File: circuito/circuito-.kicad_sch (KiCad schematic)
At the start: 15 parts, among them Q1 IRF9540 P, Q2 2N3904 / BC547, U3 TXS0108EPW, U4 TPSM53602RDA

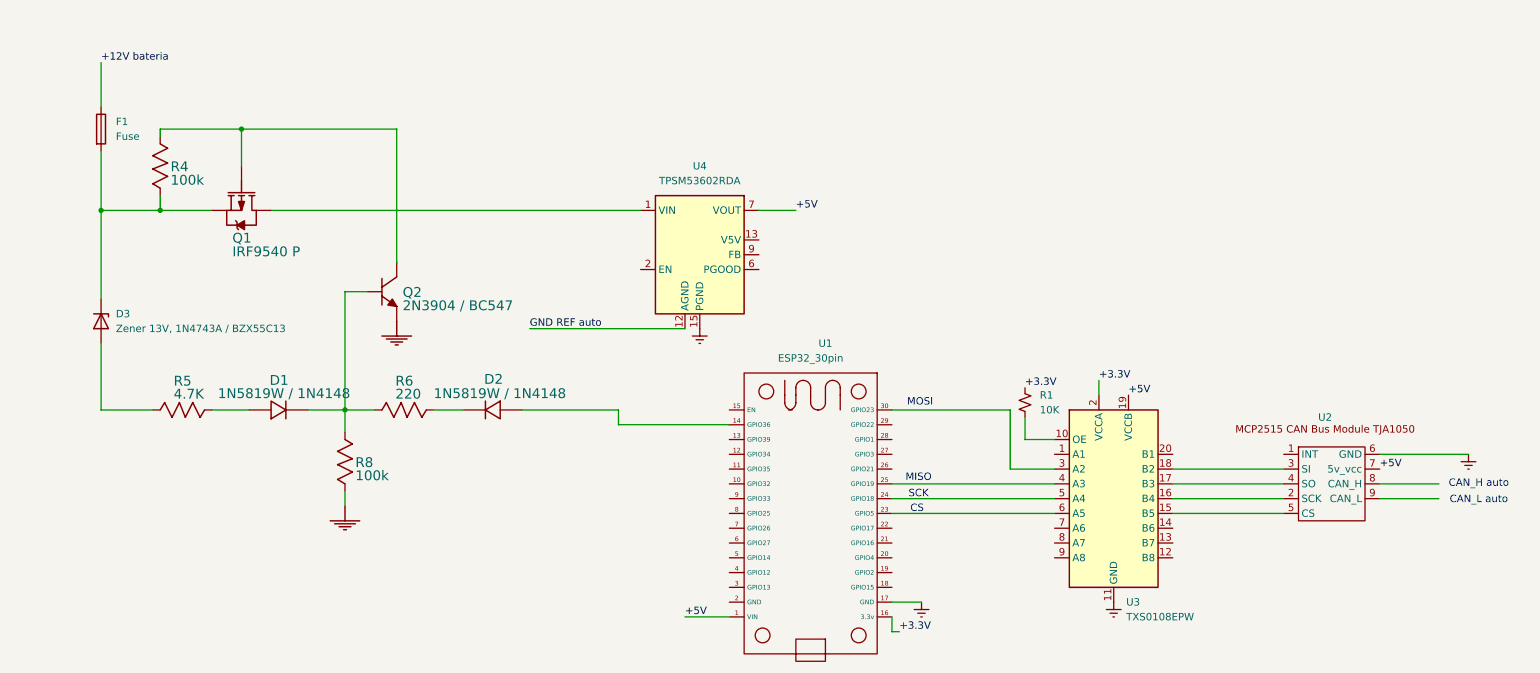
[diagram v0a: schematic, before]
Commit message: proteccion de picos del circuito, unificacion de masas
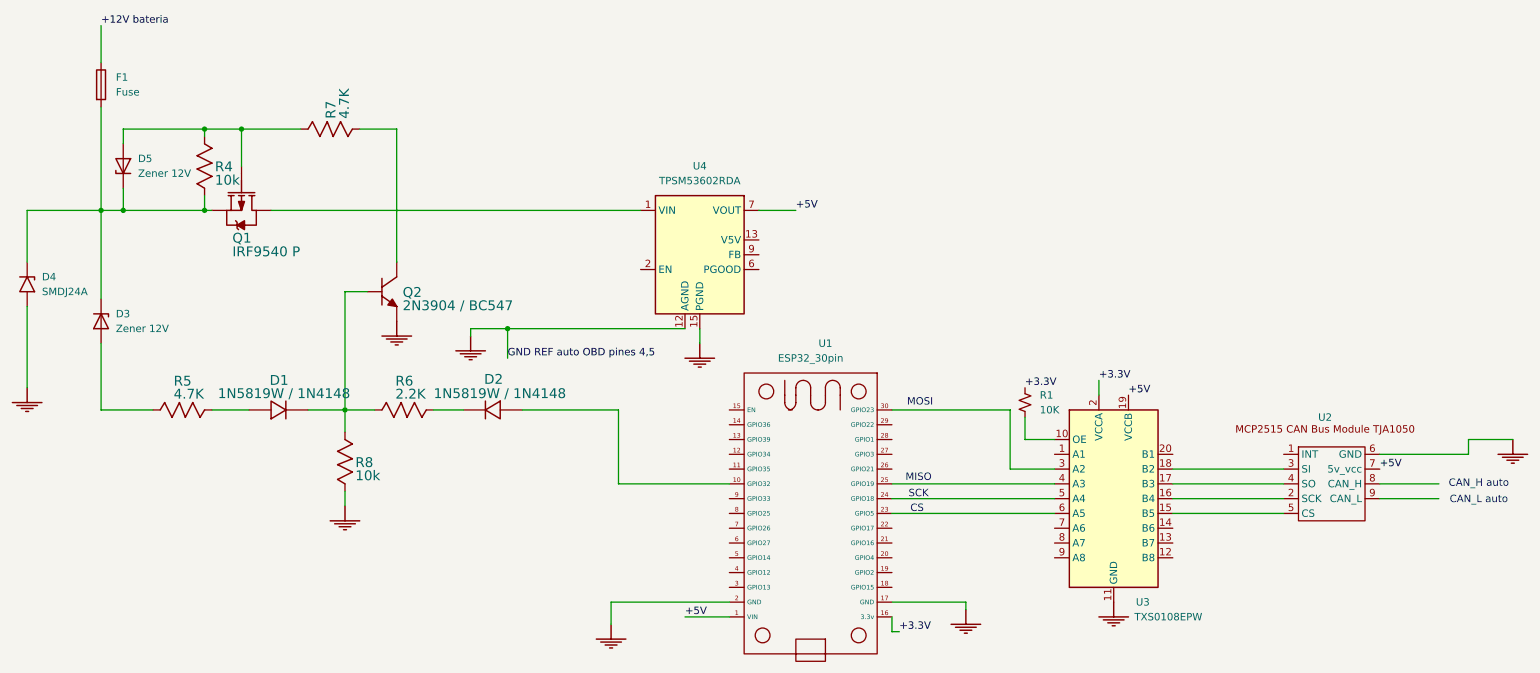
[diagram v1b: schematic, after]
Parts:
- added D4: SMDJ24A, Diode_SMD:D_SMF, symbol Diode:SMF9V0A
- added D5: Zener 12V, symbol Device:D_Zener
- added R7: 4.7K, symbol Res_AXIAL-0.3(1/8W)_US_1
- D3: value Zener 13V, 1N4743A / BZX55C13 -> Zener 12V
- R4, R8: value 100k -> 10k
- R6: value 220 -> 2.2K
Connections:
- net GND REF auto is gone; now on net GND: U4.12 (AGND)
- net GNDREF is gone; now on net GND: U1.17 (GND), U2.6 (GND), U3.11 (GND), U4.10 (PGND), U4.11 (PGND), U4.15 (PGND), U4.3 (PGND)
- net GND: now also U1.2 (GND), D4.2 (A2)
- net at Q1.1 (G), R4.1: now also D5.2 (A), R7.1; no longer Q2.3 (C)
- net at D2.1 (A): now also U1.10 (GPIO32); no longer U1.14 (GPIO36)
- net at D3.1 (K), F1.2, Q1.2 (S)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: now also D4.1 (A1), D5.1 (K)
- new net: Q2.3 (C), R7.2
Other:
- moved on the sheet: F1, R4
